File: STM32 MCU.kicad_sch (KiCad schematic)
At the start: 33 parts, among them SW3 SW_Push, SW4 SW_Push, U2 STM32G474RETx, U4 RV-3028-C7, Y1 Crystal, Y3 Crystal

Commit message: block diagram, added flyback on LED
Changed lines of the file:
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@@
+	(wire
+		(pts
+			(xy 170.18 140.97) (xy 176.53 140.97)
+		)
+		(stroke
+			(width 0)
+			(type default)
+			(color 0 0 194 1)
+		)
+	)
 	(wire
 		(pts
@@
 	(wire
 		(pts
+			(xy 170.18 143.51) (xy 176.53 143.51)
+		)
+		(stroke
+			(width 0)
+			(type default)
+			(color 0 0 194 1)
+		)
+	)
+	(wire
+		(pts
 			(xy 73.66 88.9) (xy 73.66 91.44)
 		)
@@
 	(wire
 		(pts
+			(xy 170.18 156.21) (xy 176.53 156.21)
+		)
+		(stroke
+			(width 0)
+			(type default)
+			(color 0 0 194 1)
+		)
+	)
+	(wire
+		(pts
+			(xy 170.18 153.67) (xy 176.53 153.67)
+		)
+		(stroke
+			(width 0)
+			(type default)
+			(color 0 0 194 1)
+		)
+	)
+	(wire
+		(pts
 			(xy 68.58 25.4) (xy 68.58 27.94)
 		)
@@
 	(wire
 		(pts
+			(xy 170.18 138.43) (xy 176.53 138.43)
+		)
+		(stroke
+			(width 0)
+			(type default)
+			(color 0 0 194 1)
+		)
+	)
+	(wire
+		(pts
 			(xy 134.62 38.1) (xy 132.08 38.1)
 		)
@@
 	(wire
 		(pts
+			(xy 170.18 151.13) (xy 176.53 151.13)
+		)
+		(stroke
+			(width 0)
+			(type default)
+			(color 0 0 194 1)
+		)
+	)
+	(wire
+		(pts
 			(xy 129.54 38.1) (xy 132.08 38.1)
 		)
@@
 	(wire
 		(pts
+			(xy 170.18 146.05) (xy 176.53 146.05)
+		)
+		(stroke
+			(width 0)
+			(type default)
+			(color 0 0 194 1)
+		)
+	)
+	(wire
+		(pts
 			(xy 83.82 166.37) (xy 87.63 166.37)
 		)
@@
 			(width 0)
 			(type default)
+		)
+	)
+	(wire
+		(pts
+			(xy 170.18 148.59) (xy 176.53 148.59)
+		)
+		(stroke
+			(width 0)
+			(type default)
+			(color 0 0 194 1)
 		)
 	)
@@
 		)
 	)
-	(hierarchical_label "PC_11"
+	(hierarchical_label "SD_MODE"
 		(shape input)
 		(at 210.82 93.98 180)

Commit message: STM32 Work
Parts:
- removed BT1: Battery_Cell, Battery:BatteryHolder_Keystone_3000_1x12mm, symbol Device:Battery_Cell
- removed C37, C38: C, symbol Device:C
- removed Y3: Crystal, Package_QFP:LQFP-64_10x10mm_P0.5mm, symbol Device:Crystal
- added R56: 10k, Package_DIP:DIP-8_W7.62mm, symbol Device:R
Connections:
- net +3V3: now also R56.1
- net INT_RTC: now also U2.25 (PB1), R56.2
- net TEST_LED: now also U2.24 (PB0)
- net INT_TEMP_ALERT: now reaches U2.26 (PB2)
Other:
- note removed: "CRYSTAL RTC"
- moved on the sheet: R3, R4, U4

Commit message: Revert "Merge branch 'main' of https://github.com/pequeno212/PCB_SeniorDesign_team20"
This reverts commit 8ddd870afa6ea88a1f78691f7845b0b29e49b9ae, reversing
changes made to b7b9844e80cb26773f88e7278ccd95378529a98d.
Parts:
- removed R56: 10k, Package_DIP:DIP-8_W7.62mm, symbol Device:R
- added BT1: Battery_Cell, Battery:BatteryHolder_Keystone_3000_1x12mm, symbol Device:Battery_Cell
- added C37, C38: C, symbol Device:C
- added Y3: Crystal, Package_QFP:LQFP-64_10x10mm_P0.5mm, symbol Device:Crystal
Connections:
- net GND: now also BT1.2 (-), C37.2, C38.2
- net INT_RTC: no longer U2.25 (PB1)
- net RTC_CLK_IN: now also C37.1, Y3.2
- net RTC_CLK_OUT: now also C38.1, Y3.1
- net TEST_LED: no longer U2.24 (PB0)
- net at U4.6 (VBACKUP): now also BT1.1 (+)
- net INT_TEMP_ALERT: no longer names the net of U2.26 (PB2)
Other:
- note added: "CRYSTAL RTC"
- moved on the sheet: R3, R4, U4

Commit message: Major Changes - Schematic Done??
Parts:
- removed BT1: Battery_Cell, Battery:BatteryHolder_Keystone_3000_1x12mm, symbol Device:Battery_Cell
- removed C32: 1u, symbol Device:C
- removed C37, C38: C, symbol Device:C
- removed R20: 10k, Package_DIP:DIP-8_W7.62mm, symbol Device:R
- removed SW3: SW_Push, Package_DIP:DIP-8_W7.62mm, symbol Switch:SW_Push
- removed Y3: Crystal, Package_QFP:LQFP-64_10x10mm_P0.5mm, symbol Device:Crystal
- added C10, C42: 100n, Capacitor_SMD:C_0603_1608Metric, symbol Device:C
- added J11, J5: Conn_01x02_Pin, Connector_PinHeader_2.54mm:PinHeader_1x02_P2.54mm_Vertical, symbol Connector:Conn_01x02_Pin
- added J4: Conn_01x04_Pin, Connector_PinHeader_2.54mm:PinHeader_1x04_P2.54mm_Vertical, symbol Connector:Conn_01x04_Pin
- added R12, R13, R14: 0R, Resistor_SMD:R_0603_1608Metric, symbol Device:R
- added R18, R7: 10k, Resistor_SMD:R_0603_1608Metric, symbol Device:R
- added R37: 1k, Resistor_SMD:R_0603_1608Metric, symbol Device:R
- added SW5: SW_Push, Button_Switch_THT:SW_PUSH_6mm, symbol Switch:SW_Push
- C1: renamed from C10; footprint (none) -> Capacitor_SMD:C_0603_1608Metric
- C11: renamed from C33; value 1u -> 100n; footprint (none) -> Capacitor_SMD:C_0603_1608Metric
- C2: renamed from C4; footprint (none) -> Capacitor_SMD:C_0603_1608Metric
- C3: renamed from C5; footprint (none) -> Capacitor_SMD:C_0603_1608Metric
- C4: renamed from C6; footprint (none) -> Capacitor_SMD:C_0603_1608Metric
- C5: renamed from C7; footprint (none) -> Capacitor_SMD:C_0603_1608Metric
- C6: renamed from C8; footprint (none) -> Capacitor_SMD:C_0603_1608Metric
- C7: renamed from C9; footprint (none) -> Capacitor_SMD:C_0603_1608Metric
- C8: renamed from C3; value C -> 22p; footprint (none) -> Capacitor_SMD:C_0603_1608Metric
- C9: renamed from C11; value C -> 22p; footprint (none) -> Capacitor_SMD:C_0603_1608Metric
- D1: renamed from D6; footprint (none) -> LED_SMD:LED_0603_1608Metric
- D2: renamed from D9; footprint (none) -> LED_SMD:LED_0603_1608Metric
- R10: renamed from R4; value R -> 10k; footprint Package_DIP:DIP-8_W7.62mm -> Resistor_SMD:R_0603_1608Metric
- R11: renamed from R48; footprint Package_DIP:DIP-8_W7.62mm -> Resistor_SMD:R_0603_1608Metric
- R15: renamed from R55; footprint Package_DIP:DIP-8_W7.62mm -> Resistor_SMD:R_0603_1608Metric
- R17: renamed from R19; footprint Package_DIP:DIP-8_W7.62mm -> Resistor_SMD:R_0603_1608Metric
- R19: renamed from R21; value 10k -> 1k; footprint Package_DIP:DIP-8_W7.62mm -> Resistor_SMD:R_0603_1608Metric
- R4: renamed from R36; footprint Package_DIP:DIP-8_W7.62mm -> Resistor_SMD:R_0603_1608Metric
- R5: renamed from R46; footprint Package_DIP:DIP-8_W7.62mm -> Resistor_SMD:R_0603_1608Metric
- R6: renamed from R47; footprint Package_DIP:DIP-8_W7.62mm -> Resistor_SMD:R_0603_1608Metric
- R8: footprint Package_DIP:DIP-8_W7.62mm -> Resistor_SMD:R_0603_1608Metric
- R9: renamed from R3; value R -> 7k; footprint Package_DIP:DIP-8_W7.62mm -> Resistor_SMD:R_0603_1608Metric
- SW2: renamed from SW4; footprint Package_DIP:DIP-8_W7.62mm -> Button_Switch_THT:SW_PUSH_6mm
- Y1: value Crystal -> 16MHz; footprint Package_QFP:LQFP-64_10x10mm_P0.5mm -> Crystal:Crystal_SMD_ECS_CSM3X-2Pin_7.6x4.1mm
- renumbered U4 to U2, U2 to U3
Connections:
- net BOOT0: now also J4.2 (Pin_2); no longer R17.2
- net FAN_PWM: now also U3.23 (PC5); no longer U3.9 (PC1)
- net GND: now also R17.2, C10.2, C42.2, J11.1 (Pin_1), SW5.2; no longer SW2.2
- net I2C3_SCL: now also J5.2 (Pin_2)
- net I2C3_SDA: now also J5.1 (Pin_1)
- net I2S3_CK: now also U3.52 (PC10); no longer U3.35 (PB13)
- net I2S3_SD: now also U3.54 (PC12); no longer U3.37 (PB15)
- net I2S3_WS: now also U3.51 (PA15); no longer U3.34 (PB12)
- net INT_RTC: now also R8.2, U3.38 (PC6)
- net MATRIX_A: now also U3.30 (PB10)
- net MATRIX_B: now also U3.26 (PB2)
- net MATRIX_B1: now also U3.59 (PB6)
- net MATRIX_B2: now also U3.62 (PB9)
- net MATRIX_C: now also U3.33 (PB11)
- net MATRIX_CLK: now also U3.44 (PA10)
- net MATRIX_D: now also U3.56 (PB3)
- net MATRIX_G1: now also U3.24 (PB0)
- net MATRIX_G2: now also U3.25 (PB1)
- net MATRIX_LAT: now also U3.57 (PB4)
- net MATRIX_OE: now also U3.36 (PB14)
- net MATRIX_R1: now also U3.58 (PB5)
- net MATRIX_R2: now also U3.60 (PB7)
- net PAPIR: now also U3.40 (PC8)
- net SWDCLK: now also J4.3 (Pin_3)
- net SWDIO: now also J4.4 (Pin_4)
- net TEST_LED: now also U3.39 (PC7)
- net nRST: now also C42.1, J4.1 (Pin_1), R37.1; no longer R8.2
- net at R19.2, SW2.1: now also R17.1
- net at U2.6 (VBACKUP): now also R7.2
- net LEFT_SD_MODE: now reaches U3.10 (PC2)
- net RIGHT_SD_MODE: now reaches U3.11 (PC3)
- net INT_TEMP_ALERT: now reaches U3.2 (PC13)
- net 3V3: now reaches U3.28 (VREF+)
- net 3V3: now also C1.1, C2.1, C3.1, C4.1, C5.1, C6.1, C7.1, R15.1, R4.1, R5.2, R6.2, R8.1, SW2.2, U2.7 (VDD), U3.1 (VBAT), U3.16 (VDD), U3.29 (VDDA), U3.32 (VDD), U3.48 (VDD), U3.64 (VDD), C10.1, J11.2 (Pin_2), R18.1, R7.1
- net MATRIX_PWR_EN: now reaches U3.41 (PC9)
- removed net +3V3: C1.1, C2.1, C3.1, C4.1, C5.1, C6.1, C7.1, R15.1, R17.1, R4.1, R5.2, R6.2, R8.1, U2.7 (VDD), U3.1 (VBAT), U3.16 (VDD), U3.29 (VDDA), U3.32 (VDD), U3.48 (VDD), U3.64 (VDD)
- net EXT_TEMP renamed SPI_CS_SD_CARD
- net MIC_ADC renamed MIC
- net RTC_CLK_IN: no longer names the net of U3.3 (PC14)
- net RTC_CLK_OUT: no longer names the net of U3.4 (PC15)
- net SPI_MISO: no longer names the net of U3.20 (PA6)
- net SPI_MISO: now also R13.1
- net SPI_MOSI: no longer names the net of U3.21 (PA7)
- net SPI_MOSI: now also R12.1
- net SPI_SCLK: no longer names the net of U3.19 (PA5)
- net SPI_SCLK: now also R14.1
- net TV_IR_PWM renamed TV_IR_PWM_1
- net USB_D_N renamed STM32_USB_D_N
- net USB_D_P renamed STM32_USB_D_P
- new net: R18.2, R37.2, SW5.1
- new net I2S2_CK: U3.35 (PB13)
- new net I2S2_SD: U3.37 (PB15)
- new net I2S2_WS: U3.34 (PB12)
- new net SPI1_MISO: R13.2
- new net SPI1_MOSI: R12.2
- new net SPI1_SCLK: R14.2
- new net TV_IR_PWM_2: U3.9 (PC1)
- no-connect marks 1 -> 4
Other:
- note added: "BREAKOUTS"
- note added: "STM32 POWER"
- note added: "STM32G4 MCU"
- note removed: "CRYSTAL RTC"
- moved on the sheet: C1, C11, C2, C3, C4, C5, C6, C7, C8, C9, D1, D2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

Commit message: PCB Start, Schematic polish
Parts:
- removed R7, R8: 10k, Resistor_SMD:R_0603_1608Metric, symbol Device:R
- removed U2: RV-3028-C7, Package_SON:MicroCrystal_C7_SON-8_1.5x3.2mm_P0.9mm, symbol Timer_RTC:RV-3028-C7
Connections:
- no-connect marks 4 -> 3
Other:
- note removed: "REAL TIME CLOCK"

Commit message: Basic STM + ESP Routing
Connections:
- net MATRIX_A: now also U3.56 (PB3); no longer U3.30 (PB10)
- net MATRIX_B1: now also U3.62 (PB9); no longer U3.59 (PB6)
- net MATRIX_B2: now also U3.60 (PB7); no longer U3.62 (PB9)
- net MATRIX_C: now also U3.57 (PB4); no longer U3.33 (PB11)
- net MATRIX_D: now also U3.30 (PB10); no longer U3.56 (PB3)
- net MATRIX_LAT: now also U3.33 (PB11); no longer U3.57 (PB4)
- net MATRIX_R1: now also U3.59 (PB6); no longer U3.58 (PB5)
- net MATRIX_R2: now also U3.58 (PB5); no longer U3.60 (PB7)

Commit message: Almost Done with Dev Board
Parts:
- removed D1: LED, LED_SMD:LED_0603_1608Metric, symbol Device:LED
- removed J11: Conn_01x02_Pin, Connector_PinHeader_2.54mm:PinHeader_1x02_P2.54mm_Vertical, symbol Connector:Conn_01x02_Pin
- removed R4: 330, Resistor_SMD:R_0603_1608Metric, symbol Device:R
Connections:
- net LEFT_SD_MODE: now also U3.11 (PC3); no longer U3.10 (PC2)
- net RIGHT_SD_MODE: now also U3.10 (PC2); no longer U3.11 (PC3)

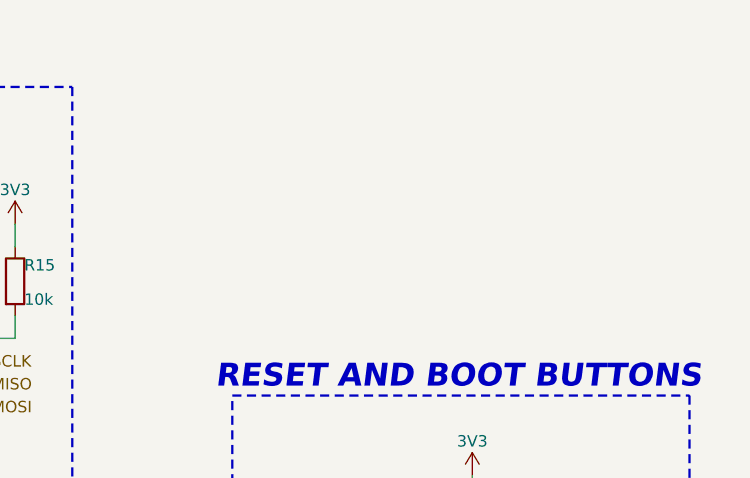
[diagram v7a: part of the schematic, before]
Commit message: connectors changed from headers, added SWD conn
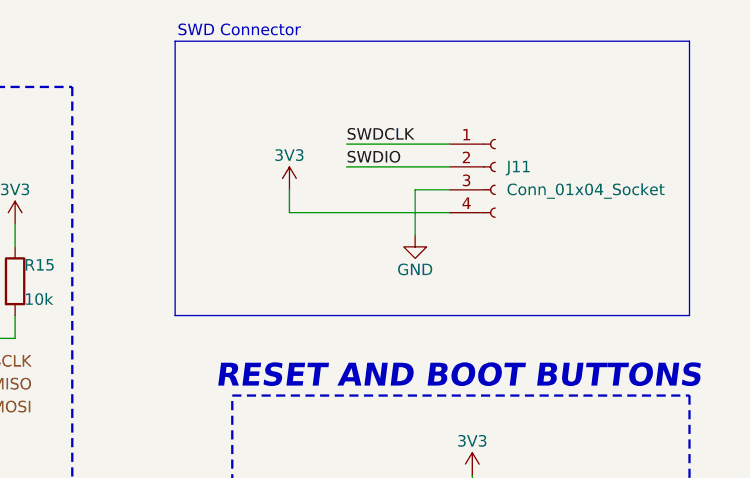
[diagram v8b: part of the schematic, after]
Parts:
- added J11: Conn_01x04_Socket, Connector_Molex:Molex_SL_171971-0004_1x04_P2.54mm_Vertical, symbol Connector:Conn_01x04_Socket
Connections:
- net 3V3: now also J11.4 (Pin_4)
- net GND: now also J11.3 (Pin_3)
- net SWDCLK: now also J11.1 (Pin_1)
- net SWDIO: now also J11.2 (Pin_2)
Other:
- note added: "SWD Connector"
